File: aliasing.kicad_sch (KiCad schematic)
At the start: 15 parts, among them J1001 Conn_Coaxial, J1002 Conn_Coaxial, J1003 Conn_Coaxial, J1004 Conn_Coaxial, J1005 Conn_Coaxial, J1006 Conn_Coaxial, J1007 Conn_01x01_Female, J1008 Conn_01x01_Female, J1009 Conn_01x01_Female, J1010 Conn_01x01_Female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

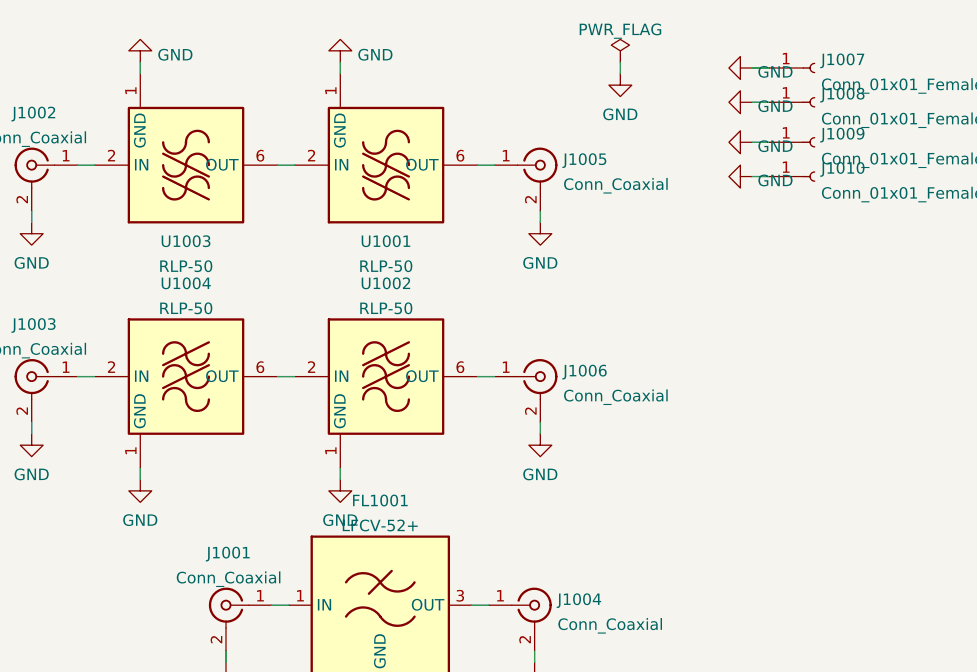
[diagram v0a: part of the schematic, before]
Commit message: TLV diodes added, new gerber, minor modif.
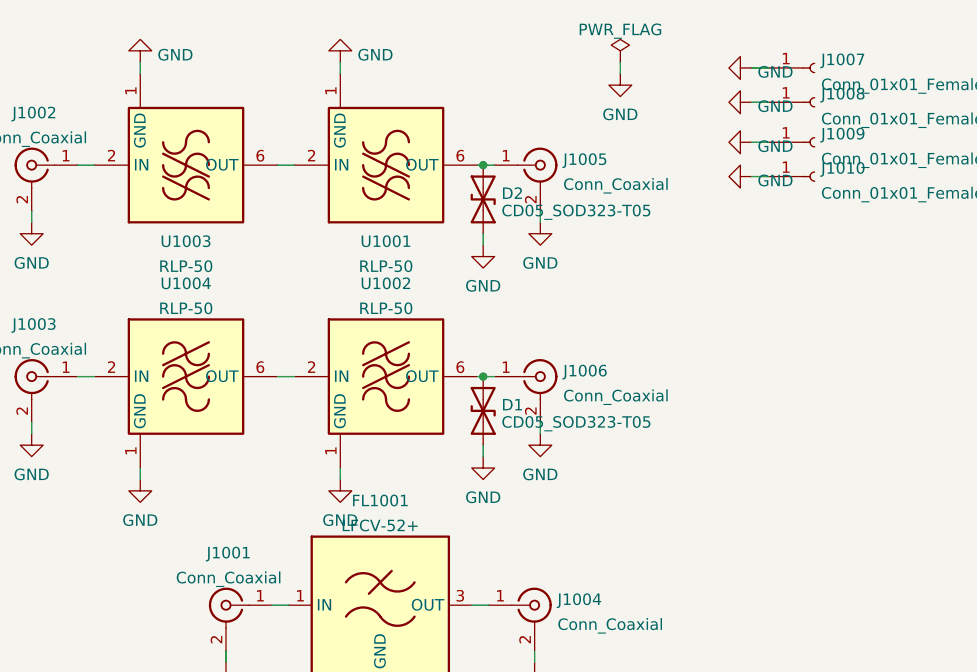
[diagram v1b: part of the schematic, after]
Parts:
- added D1, D2: CD05_SOD323-T05, Diode_SMD:D_SOD-323, symbol Diode:1.5KExxCA
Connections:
- net GND: now also D1.1 (A1), D2.1 (A1)
- net at J1006.1 (In), U1002.6 (OUT): now also D1.2 (A2)
- net at J1005.1 (In), U1001.6 (OUT): now also D2.2 (A2)
